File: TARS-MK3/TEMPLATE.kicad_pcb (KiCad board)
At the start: 2 copper layers, 88.3 x 88.3 mm, 4 parts, among them J1 Conn_02x12_Odd_Even, J2 Conn_02x12_Odd_Even, J3 Conn_02x12_Odd_Even, J4 Conn_02x12_Odd_Even

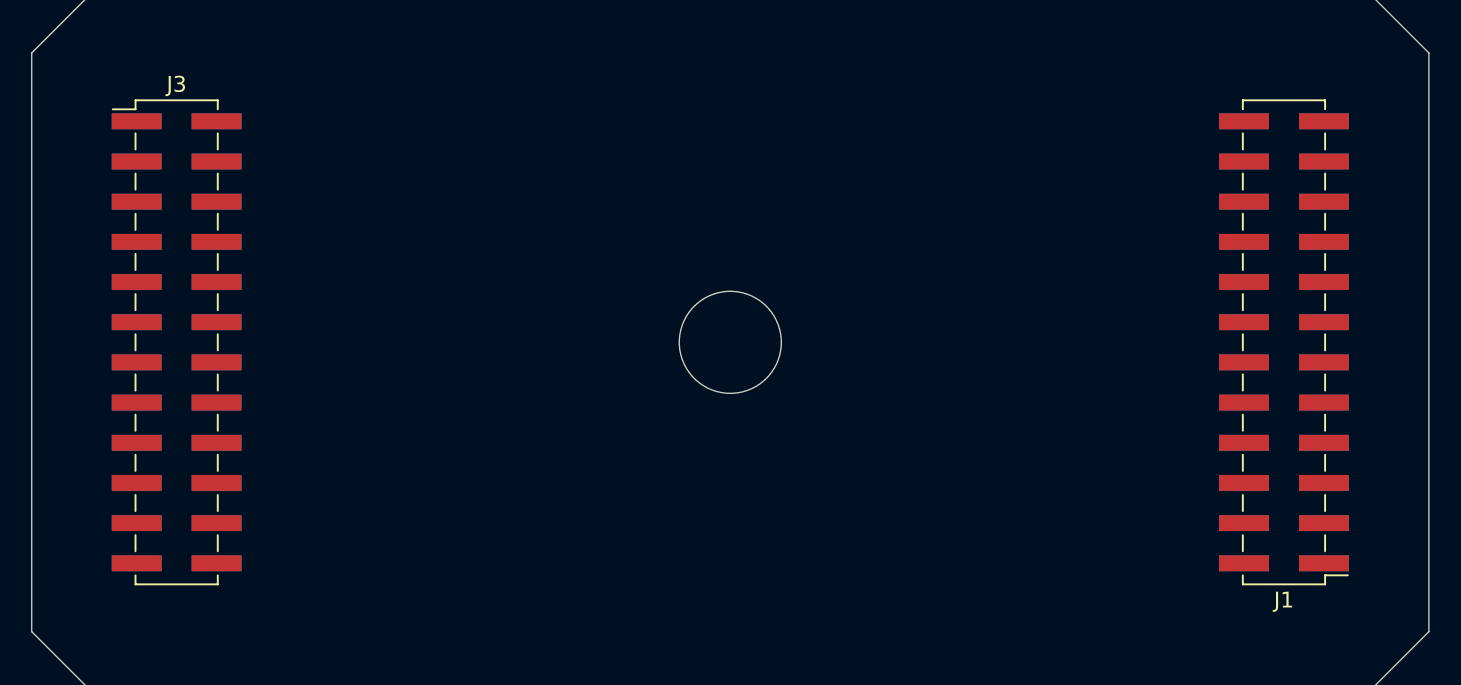
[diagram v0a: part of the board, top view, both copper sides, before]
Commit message: Added vias for B2B
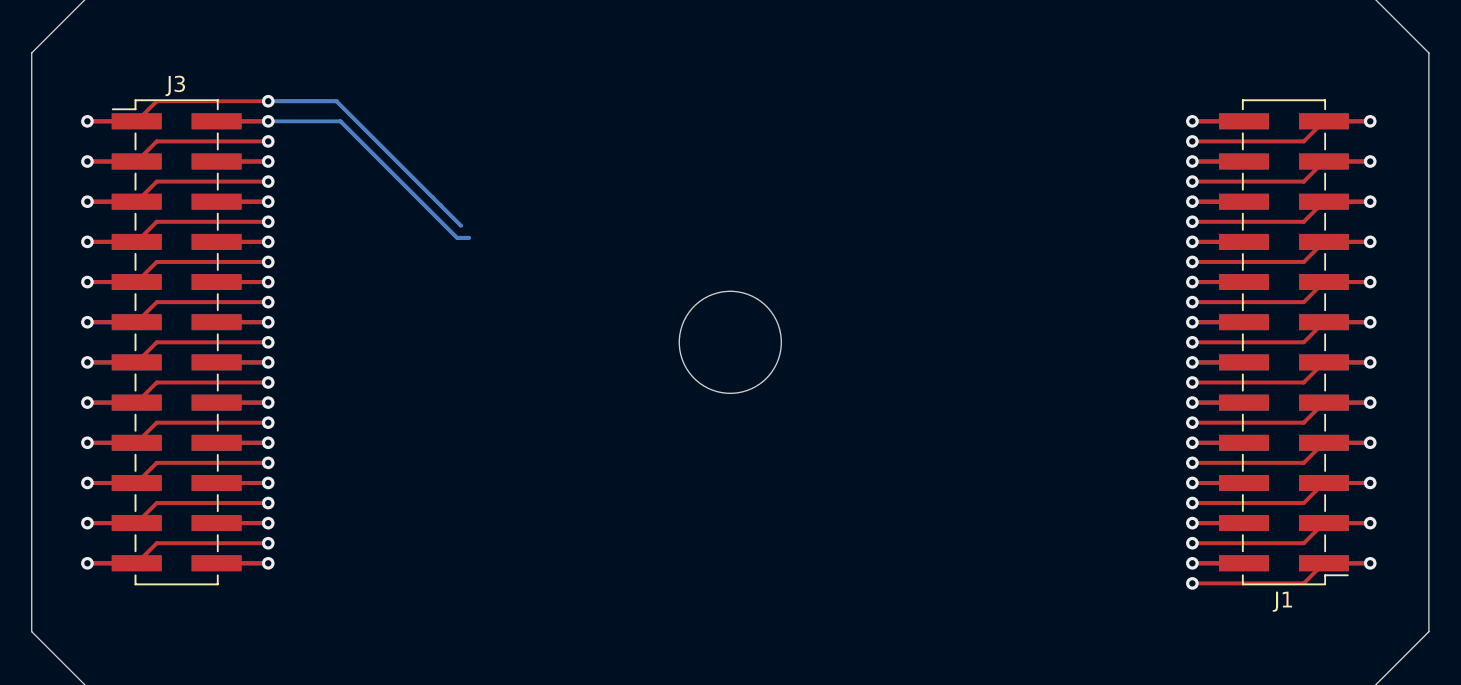
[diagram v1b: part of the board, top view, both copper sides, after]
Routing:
- net /VBAT: track 0.00 -> 45.6 mm, vias 0 -> 4
- net /CONT: track 0.00 -> 30.1 mm, vias 0 -> 4
- net /B2B_UART_RX: track 0.00 -> 30.1 mm, vias 0 -> 4
- net /B2B_SPI_SCK: track 0.00 -> 30.1 mm, vias 0 -> 4
- net /B2B_SPI_MOSI: track 0.00 -> 30.1 mm, vias 0 -> 4
- net /B2B_I2C_SDA: track 0.00 -> 30.1 mm, vias 0 -> 4
- net /9V: track 0.00 -> 30.1 mm, vias 0 -> 4
- net /5V: track 0.00 -> 30.1 mm, vias 0 -> 4
- net /3V3: track 0.00 -> 30.1 mm, vias 0 -> 4
- net /B2B_UART_TX: track 0.00 -> 30.1 mm, vias 0 -> 4
- net /B2B_SPI_MISO: track 0.00 -> 30.1 mm, vias 0 -> 4
- net /B2B_I2C_SCL: track 0.00 -> 30.1 mm, vias 0 -> 4
- net /B2B_GPIO_0: track 0.00 -> 28.8 mm, vias 0 -> 2
- net /B2B_GPIO_9: track 0.00 -> 13.1 mm, vias 0 -> 2
- net /B2B_GPIO_8: track 0.00 -> 13.1 mm, vias 0 -> 2
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
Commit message: save point 1
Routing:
- net /B2B_GPIO_11: track 13.1 -> 50.1 mm
- net /B2B_SPI_MOSI: track 30.1 -> 66.9 mm
- net /B2B_UART_TX: track 30.1 -> 66.7 mm
- net /B2B_GPIO_10: track 13.1 -> 49.5 mm
- net /B2B_GPIO_6: track 13.1 -> 49.3 mm
- net /B2B_SPI_MISO: track 30.1 -> 66.2 mm
- net /B2B_I2C_SDA: track 30.1 -> 66.0 mm
- net /B2B_GPIO_9: track 13.1 -> 48.8 mm
- net /B2B_GPIO_7: track 13.1 -> 48.6 mm
- net /B2B_SPI_SCK: track 30.1 -> 65.6 mm
- net /B2B_I2C_SCL: track 30.1 -> 65.4 mm
- net /B2B_GPIO_8: track 13.1 -> 48.2 mm
- net /B2B_GPIO_0: track 28.8 -> 13.1 mm
- net /VBAT: track 45.6 -> 30.1 mm
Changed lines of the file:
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@@
   (via (at 40.453 13.97) (size 0.8) (drill 0.4) (layers "F.Cu" "B.Cu") (net 1))
   (via (at -40.64 -13.97) (size 0.8) (drill 0.4) (layers "F.Cu" "B.Cu") (net 1))
-  (segment (start -29.21 -15.24) (end -24.892 -15.24) (width 0.25) (layer "B.Cu") (net 1))
-  (segment (start -24.892 -15.24) (end -18.796 -9.144) (width 0.25) (layer "B.Cu") (net 1))
-  (segment (start -18.288 -8.636) (end -17.018 -7.366) (width 0.25) (layer "B.Cu") (net 1))
   (segment (start 37.338 13.97) (end 40.453 13.97) (width 0.25) (layer "B.Cu") (net 1))
-  (segment (start -18.796 -9.144) (end -18.288 -8.636) (width 0.25) (layer "B.Cu") (net 1))
   (segment (start -37.525 -13.97) (end -40.64 -13.97) (width 0.25) (layer "B.Cu") (net 1))
   (segment (start 32.475 13.97) (end 29.21 13.97) (width 0.25) (layer "F.Cu") (net 2))
@@
   (via (at -29.21 -13.97) (size 0.8) (drill 0.4) (layers "F.Cu" "B.Cu") (net 2))
   (via (at 29.21 13.97) (size 0.8) (drill 0.4) (layers "F.Cu" "B.Cu") (net 2))
-  (segment (start -29.21 -13.97) (end -24.638 -13.97) (width 0.25) (layer "B.Cu") (net 2))
   (segment (start -29.21 -13.97) (end -32.475 -13.97) (width 0.25) (layer "B.Cu") (net 2))
-  (segment (start -24.638 -13.97) (end -17.272 -6.604) (width 0.25) (layer "B.Cu") (net 2))
-  (segment (start -17.272 -6.604) (end -16.51 -6.604) (width 0.25) (layer "B.Cu") (net 2))
   (segment (start 29.21 13.97) (end 32.475 13.97) (width 0.25) (layer "B.Cu") (net 2))
   (segment (start -36.255 -12.7) (end -29.21 -12.7) (width 0.25) (layer "F.Cu") (net 3))
@@
   (via (at 29.21 0) (size 0.8) (drill 0.4) (layers "F.Cu" "B.Cu") (net 13))
   (via (at 40.453 -1.27) (size 0.8) (drill 0.4) (layers "F.Cu" "B.Cu") (net 13))
+  (segment (start -27.686 0) (end -24.13 3.556) (width 0.25) (layer "B.Cu") (net 13))
   (segment (start -37.525 1.27) (end -40.64 1.27) (width 0.25) (layer "B.Cu") (net 13))
   (segment (start 37.338 -1.27) (end 40.453 -1.27) (width 0.25) (layer "B.Cu") (net 13))
+  (segment (start -24.13 3.556) (end 5.842 3.556) (width 0.25) (layer "B.Cu") (net 13))
+  (segment (start -29.21 0) (end -27.686 0) (width 0.25) (layer "B.Cu") (net 13))
   (segment (start -32.475 1.27) (end -29.21 1.27) (width 0.25) (layer "F.Cu") (net 14))
   (segment (start 32.475 -1.27) (end 29.21 -1.27) (width 0.25) (layer "F.Cu") (net 14))
@@
   (via (at 29.21 -1.27) (size 0.8) (drill 0.4) (layers "F.Cu" "B.Cu") (net 14))
   (segment (start -29.21 1.27) (end -32.475 1.27) (width 0.25) (layer "B.Cu") (net 14))
+  (segment (start -29.21 1.27) (end -27.432 1.27) (width 0.25) (layer "B.Cu") (net 14))
   (segment (start 29.21 -1.27) (end 32.475 -1.27) (width 0.25) (layer "B.Cu") (net 14))
+  (segment (start -27.432 1.27) (end -24.638 4.064) (width 0.25) (layer "B.Cu") (net 14))
+  (segment (start -24.638 4.064) (end 5.842 4.064) (width 0.25) (layer "B.Cu") (net 14))
   (segment (start 37.338 -3.81) (end 40.453 -3.81) (width 0.25) (layer "F.Cu") (net 15))
   (segment (start -37.525 3.81) (end -36.255 2.54) (width 0.25) (layer "F.Cu") (net 15))
@@
   (via (at -40.64 3.81) (size 0.8) (drill 0.4) (layers "F.Cu" "B.Cu") (net 15))
   (via (at -29.21 2.54) (size 0.8) (drill 0.4) (layers "F.Cu" "B.Cu") (net 15))
+  (segment (start -29.21 2.54) (end -27.432 2.54) (width 0.25) (layer "B.Cu") (net 15))
+  (segment (start -25.4 4.572) (end 5.842 4.572) (width 0.25) (layer "B.Cu") (net 15))
   (segment (start -40.64 3.81) (end -37.525 3.81) (width 0.25) (layer "B.Cu") (net 15))
+  (segment (start -27.432 2.54) (end -25.4 4.572) (width 0.25) (layer "B.Cu") (net 15))
   (segment (start 40.453 -3.81) (end 37.338 -3.81) (width 0.25) (layer "B.Cu") (net 15))
   (segment (start 29.21 -3.81) (end 32.475 -3.81) (width 0.25) (layer "F.Cu") (net 16))
@@
   (via (at -29.21 3.81) (size 0.8) (drill 0.4) (layers "F.Cu" "B.Cu") (net 16))
   (via (at 29.21 -3.81) (size 0.8) (drill 0.4) (layers "F.Cu" "B.Cu") (net 16))
+  (segment (start -27.178 3.81) (end -25.908 5.08) (width 0.25) (layer "B.Cu") (net 16))
   (segment (start -32.475 3.81) (end -29.21 3.81) (width 0.25) (layer "B.Cu") (net 16))
+  (segment (start -29.21 3.81) (end -27.178 3.81) (width 0.25) (layer "B.Cu") (net 16))
+  (segment (start -25.908 5.08) (end 5.842 5.08) (width 0.25) (layer "B.Cu") (net 16))
   (segment (start 32.475 -3.81) (end 29.21 -3.81) (width 0.25) (layer "B.Cu") (net 16))
   (segment (start -36.255 5.08) (end -29.21 5.08) (width 0.25) (layer "F.Cu") (net 17))
@@
   (via (at -40.64 6.35) (size 0.8) (drill 0.4) (layers "F.Cu" "B.Cu") (net 17))
   (segment (start -37.525 6.35) (end -40.64 6.35) (width 0.25) (layer "B.Cu") (net 17))
+  (segment (start -26.67 5.588) (end 5.842 5.588) (width 0.25) (layer "B.Cu") (net 17))
+  (segment (start -27.178 5.08) (end -26.67 5.588) (width 0.25) (layer "B.Cu") (net 17))
   (segment (start 37.338 -6.35) (end 40.453 -6.35) (width 0.25) (layer "B.Cu") (net 17))
+  (segment (start -29.21 5.08) (end -27.178 5.08) (width 0.25) (layer "B.Cu") (net 17))
   (segment (start 32.475 -6.35) (end 29.21 -6.35) (width 0.25) (layer "F.Cu") (net 18))
   (segment (start -32.475 6.35) (end -29.21 6.35) (width 0.25) (layer "F.Cu") (net 18))
   (via (at 29.21 -6.35) (size 0.8) (drill 0.4) (layers "F.Cu" "B.Cu") (net 18))
   (via (at -29.21 6.35) (size 0.8) (drill 0.4) (layers "F.Cu" "B.Cu") (net 18))
+  (segment (start -29.21 6.35) (end -26.924 6.35) (width 0.25) (layer "B.Cu") (net 18))
+  (segment (start -26.924 6.35) (end -26.67 6.096) (width 0.25) (layer "B.Cu") (net 18))
+  (segment (start -26.67 6.096) (end 5.842 6.096) (width 0.25) (layer "B.Cu") (net 18))
   (segment (start 29.21 -6.35) (end 32.475 -6.35) (width 0.25) (layer "B.Cu") (net 18))
   (segment (start -29.21 6.35) (end -32.475 6.35) (width 0.25) (layer "B.Cu") (net 18))
@@
   (segment (start 40.453 -8.89) (end 37.338 -8.89) (width 0.25) (layer "B.Cu") (net 19))
   (segment (start -40.64 8.89) (end -37.525 8.89) (width 0.25) (layer "B.Cu") (net 19))
+  (segment (start -29.21 7.62) (end -27.178 7.62) (width 0.25) (layer "B.Cu") (net 19))
+  (segment (start -27.178 7.62) (end -26.162 6.604) (width 0.25) (layer "B.Cu") (net 19))
+  (segment (start -26.162 6.604) (end 5.842 6.604) (width 0.25) (layer "B.Cu") (net 19))
   (segment (start -29.21 8.89) (end -32.475 8.89) (width 0.25) (layer "F.Cu") (net 20))
   (segment (start 29.21 -8.89) (end 32.475 -8.89) (width 0.25) (layer "F.Cu") (net 20))
   (via (at 29.21 -8.89) (size 0.8) (drill 0.4) (layers "F.Cu" "B.Cu") (net 20))
   (via (at -29.21 8.89) (size 0.8) (drill 0.4) (layers "F.Cu" "B.Cu") (net 20))
+  (segment (start -29.21 8.89) (end -27.432 8.89) (width 0.25) (layer "B.Cu") (net 20))
+  (segment (start -27.432 8.89) (end -25.654 7.112) (width 0.25) (layer "B.Cu") (net 20))
   (segment (start 32.475 -8.89) (end 29.21 -8.89) (width 0.25) (layer "B.Cu") (net 20))
+  (segment (start -25.654 7.112) (end 5.842 7.112) (width 0.25) (layer "B.Cu") (net 20))
   (segment (start -32.475 8.89) (end -29.21 8.89) (width 0.25) (layer "B.Cu") (net 20))
   (segment (start -40.64 11.43) (end -37.525 11.43) (width 0.25) (layer "F.Cu") (net 21))
@@
   (via (at 29.21 -10.16) (size 0.8) (drill 0.4) (layers "F.Cu" "B.Cu") (net 21))
   (via (at -40.64 11.43) (size 0.8) (drill 0.4) (layers "F.Cu" "B.Cu") (net 21))
+  (segment (start -29.21 10.16) (end -27.686 10.16) (width 0.25) (layer "B.Cu") (net 21))
   (segment (start 37.338 -11.43) (end 40.453 -11.43) (width 0.25) (layer "B.Cu") (net 21))
+  (segment (start -27.686 10.16) (end -25.146 7.62) (width 0.25) (layer "B.Cu") (net 21))
   (segment (start -37.525 11.43) (end -40.64 11.43) (width 0.25) (layer "B.Cu") (net 21))
+  (segment (start -25.146 7.62) (end 5.842 7.62) (width 0.25) (layer "B.Cu") (net 21))
   (segment (start 32.475 -11.43) (end 29.21 -11.43) (width 0.25) (layer "F.Cu") (net 22))
   (segment (start -32.475 11.43) (end -29.21 11.43) (width 0.25) (layer "F.Cu") (net 22))
@@
   (via (at 29.21 -11.43) (size 0.8) (drill 0.4) (layers "F.Cu" "B.Cu") (net 22))
   (segment (start -29.21 11.43) (end -32.475 11.43) (width 0.25) (layer "B.Cu") (net 22))
+  (segment (start -24.638 8.128) (end 5.842 8.128) (width 0.25) (layer "B.Cu") (net 22))
+  (segment (start -29.21 11.43) (end -27.94 11.43) (width 0.25) (layer "B.Cu") (net 22))
   (segment (start 29.21 -11.43) (end 32.475 -11.43) (width 0.25) (layer "B.Cu") (net 22))
+  (segment (start -27.94 11.43) (end -24.638 8.128) (width 0.25) (layer "B.Cu") (net 22))
   (segment (start 36.255 -12.7) (end 29.21 -12.7) (width 0.25) (layer "F.Cu") (net 23))
   (segment (start -36.255 12.7) (end -29.21 12.7) (width 0.25) (layer "F.Cu") (net 23))
@@
   (via (at -29.21 12.7) (size 0.8) (drill 0.4) (layers "F.Cu" "B.Cu") (net 23))
   (segment (start -40.64 13.97) (end -37.525 13.97) (width 0.25) (layer "B.Cu") (net 23))
+  (segment (start -27.94 12.7) (end -23.876 8.636) (width 0.25) (layer "B.Cu") (net 23))
+  (segment (start -29.21 12.7) (end -27.94 12.7) (width 0.25) (layer "B.Cu") (net 23))
   (segment (start 40.453 -13.97) (end 37.338 -13.97) (width 0.25) (layer "B.Cu") (net 23))
+  (segment (start -23.876 8.636) (end 5.842 8.636) (width 0.25) (layer "B.Cu") (net 23))
   (segment (start 29.21 -13.97) (end 32.475 -13.97) (width 0.25) (layer "F.Cu") (net 24))
   (segment (start -29.21 13.97) (end -32.475 13.97) (width 0.25) (layer "F.Cu") (net 24))
@@
   (via (at 29.21 -13.97) (size 0.8) (drill 0.4) (layers "F.Cu" "B.Cu") (net 24))
   (segment (start 32.475 -13.97) (end 29.21 -13.97) (width 0.25) (layer "B.Cu") (net 24))
+  (segment (start -23.114 9.144) (end 5.842 9.144) (width 0.25) (layer "B.Cu") (net 24))
   (segment (start -32.475 13.97) (end -29.21 13.97) (width 0.25) (layer "B.Cu") (net 24))
+  (segment (start -27.94 13.97) (end -23.114 9.144) (width 0.25) (layer "B.Cu") (net 24))
+  (segment (start -29.21 13.97) (end -27.94 13.97) (width 0.25) (layer "B.Cu") (net 24))
   (group "" (id d6947100-58b3-4c9c-b7d9-dfc4b6f58c45)
     (members

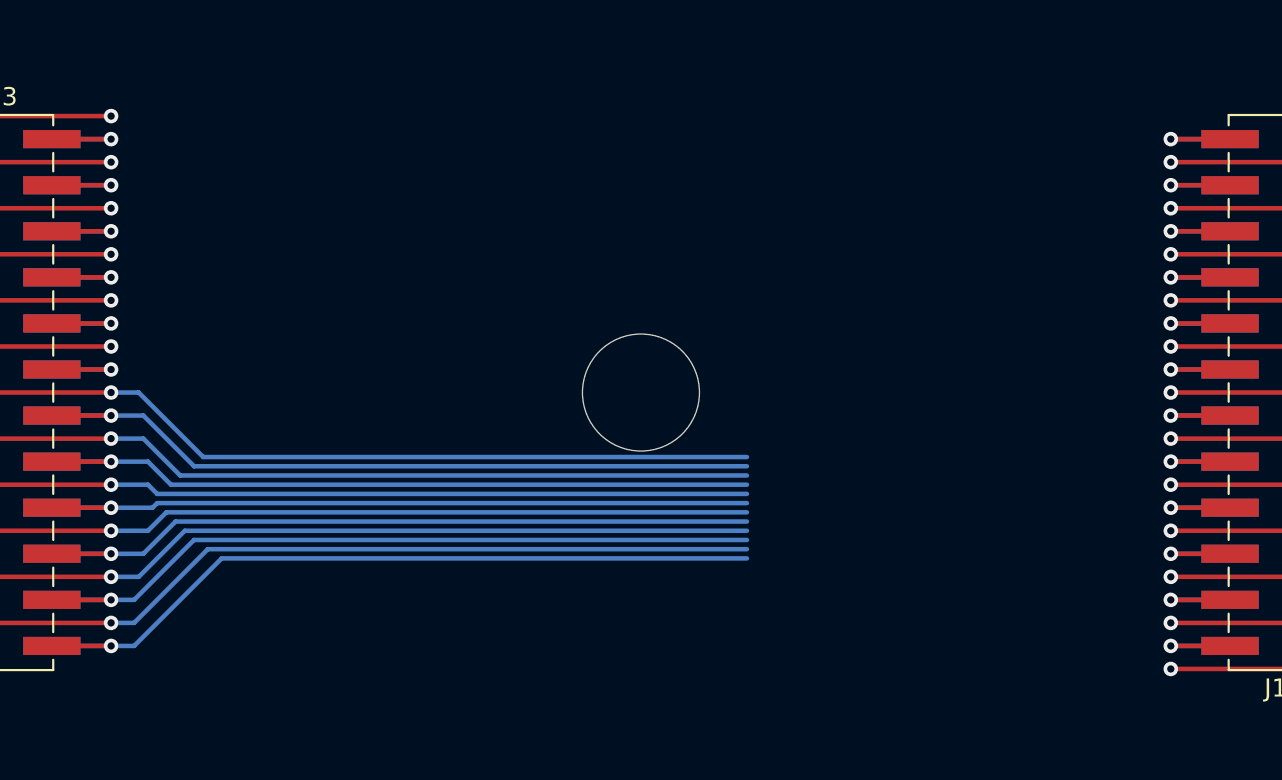
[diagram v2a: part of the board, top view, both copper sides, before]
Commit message: Routed B2Bs
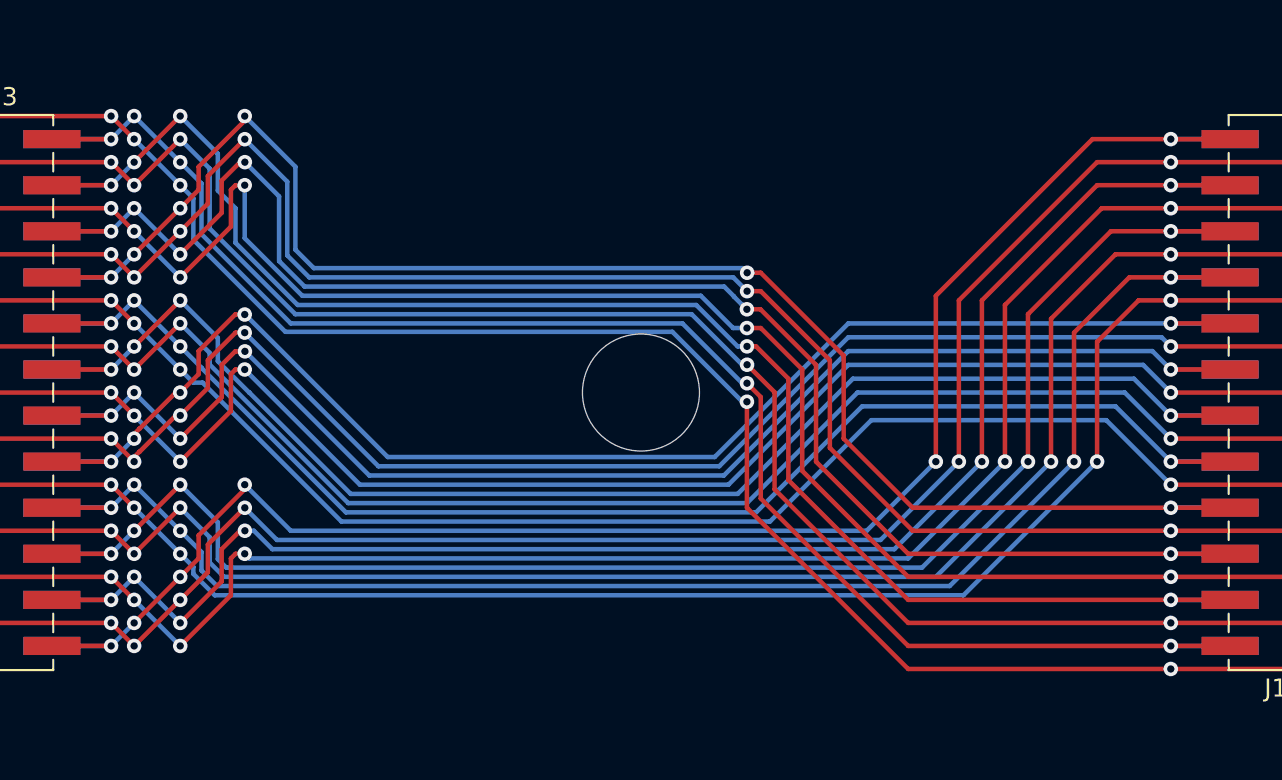
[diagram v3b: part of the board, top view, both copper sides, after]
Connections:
- net /CONT renamed /GND
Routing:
- net /B2B_GPIO_2: track 13.1 -> 90.4 mm, vias 2 -> 6
- net /B2B_GPIO_3: track 13.1 -> 90.4 mm, vias 2 -> 6
- net /5V: track 30.1 -> 107.4 mm, vias 4 -> 8
- net /3V3: track 30.1 -> 107.3 mm, vias 4 -> 8
- net /B2B_GPIO_1: track 13.1 -> 89.7 mm, vias 2 -> 5
- net /9V: track 30.1 -> 106.3 mm, vias 4 -> 7
- net /B2B_GPIO_0: track 13.1 -> 89.0 mm, vias 2 -> 5
- net /VBAT: track 30.1 -> 105.9 mm, vias 4 -> 7
- net /B2B_GPIO_5: track 13.1 -> 81.7 mm, vias 2 -> 4
- net /B2B_UART_RX: track 30.1 -> 98.2 mm, vias 4 -> 6
- net /B2B_GPIO_4: track 13.1 -> 80.5 mm, vias 2 -> 4
- net /GND: track 30.1 -> 97.4 mm, vias 4 -> 6
- net /B2B_GPIO_11: track 50.1 -> 91.4 mm, vias 2 -> 6
- net /B2B_SPI_MOSI: track 66.9 -> 107.7 mm, vias 4 -> 8
- net /B2B_GPIO_10: track 49.5 -> 90.1 mm, vias 2 -> 6
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
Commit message: Finished B2B fully
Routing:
- net /B2B_GPIO_6: track 82.4 -> 82.2 mm, vias 5 -> 4
- net /B2B_I2C_SDA: track 99.0 -> 98.9 mm, vias 7 -> 4
- net /VBAT: vias 7 -> 4
- net /GND: vias 6 -> 5
- net /B2B_UART_TX: vias 7 -> 6
- net /B2B_UART_RX: vias 6 -> 4
- net /B2B_SPI_SCK: vias 7 -> 4
- net /B2B_SPI_MOSI: vias 8 -> 4
- net /B2B_SPI_MISO: vias 8 -> 6
- net /B2B_I2C_SCL: vias 7 -> 4
- net /B2B_GPIO_8: vias 5 -> 3
- net /B2B_GPIO_7: vias 5 -> 4
- net /B2B_GPIO_4: vias 4 -> 2
- net /B2B_GPIO_3: vias 6 -> 5
- net /B2B_GPIO_2: vias 6 -> 5
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- added copper zone on B.Cu, net /GND
- added copper zone on F.Cu, net /GND

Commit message: added arduino feather and RFM96 dimensions to template board
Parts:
- moved J1 155.5 mm to (156.9, 96.5)
- moved J2 155.5 mm to (156.9, 96.5)
- moved J3 155.5 mm to (86.9, 96.5)
- moved J4 155.5 mm to (86.9, 96.5)
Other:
- board text added: "16mm x 16mm"
- board text added: "Arduino Feather"
- board text added: "RFM96 Radio module"
